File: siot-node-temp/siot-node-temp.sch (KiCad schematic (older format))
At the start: 9 parts, among them J1 Conn_01x03, J2 Conn_01x03, J3 Conn_01x03, J4 Conn_01x03, U1 L78L05_SO8

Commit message: fix hole sizes
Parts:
- J1, J4: footprint Connector_PinHeader_1.27mm:PinHeader_1x03_P1.27mm_Vertical -> bec:xConnect; symbol Connector_Generic:Conn_01x03 -> Connector:Conn_01x03_Female
- J2, J3: footprint Connector_PinHeader_1.27mm:PinHeader_1x03_P1.27mm_Vertical -> Connector_PinHeader_2.54mm:PinHeader_1x03_P2.54mm_Vertical; symbol Connector_Generic:Conn_01x03 -> Connector:Conn_01x03_Female
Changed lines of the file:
@@
 EESchema Schematic File Version 4
+LIBS:siot-node-temp-cache
 EELAYER 29 0
 EELAYER END
@@
 $EndComp
 $Comp
-L Connector_Generic:Conn_01x03 J1
+L Connector:Conn_01x03_Female J1
 U 1 1 5D321886
 P 4050 3500
 F 0 "J1" H 4200 3600 50  0000 C CNN
 F 1 "Conn_01x03" H 4050 3300 50  0000 C CNN
-F 2 "Connector_PinHeader_1.27mm:PinHeader_1x03_P1.27mm_Vertical" H 4050 3500 50  0001 C CNN
+F 2 "bec:xConnect" H 4050 3500 50  0001 C CNN
 F 3 "~" H 4050 3500 50  0001 C CNN
 	1    4050 3500
@@
 $EndComp
 $Comp
-L Connector_Generic:Conn_01x03 J4
+L Connector:Conn_01x03_Female J4
 U 1 1 5D323EF2
 P 6750 3500
 F 0 "J4" H 6830 3542 50  0000 L CNN
 F 1 "Conn_01x03" H 6550 3300 50  0000 L CNN
-F 2 "Connector_PinHeader_1.27mm:PinHeader_1x03_P1.27mm_Vertical" H 6750 3500 50  0001 C CNN
+F 2 "bec:xConnect" H 6750 3500 50  0001 C CNN
 F 3 "~" H 6750 3500 50  0001 C CNN
 	1    6750 3500
@@
 $EndComp
 $Comp
-L Connector_Generic:Conn_01x03 J2
+L Connector:Conn_01x03_Female J2
 U 1 1 5D32548C
 P 4800 2500
 F 0 "J2" V 4764 2312 50  0000 R CNN
 F 1 "Conn_01x03" V 4673 2312 50  0000 R CNN
-F 2 "Connector_PinHeader_1.27mm:PinHeader_1x03_P1.27mm_Vertical" H 4800 2500 50  0001 C CNN
+F 2 "Connector_PinHeader_2.54mm:PinHeader_1x03_P2.54mm_Vertical" H 4800 2500 50  0001 C CNN
 F 3 "~" H 4800 2500 50  0001 C CNN
 	1    4800 2500
@@
 $EndComp
 $Comp
-L Connector_Generic:Conn_01x03 J3
+L Connector:Conn_01x03_Female J3
 U 1 1 5D327365
 P 5800 2500
 F 0 "J3" V 5764 2312 50  0000 R CNN
 F 1 "Conn_01x03" V 5673 2312 50  0000 R CNN
-F 2 "Connector_PinHeader_1.27mm:PinHeader_1x03_P1.27mm_Vertical" H 5800 2500 50  0001 C CNN
+F 2 "Connector_PinHeader_2.54mm:PinHeader_1x03_P2.54mm_Vertical" H 5800 2500 50  0001 C CNN
 F 3 "~" H 5800 2500 50  0001 C CNN
 	1    5800 2500

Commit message: design updates
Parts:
- removed J1, J4: Conn_01x03, bec:xConnect, symbol Connector:Conn_01x03_Female
- removed U1: L78L05_SO8, Package_SO:SOIC-8_3.9x4.9mm_P1.27mm, symbol Regulator_Linear:L78L05_SO8
- added J1, J4: xConnect_smd, BEC:xConnect_smd, symbol bec-connector:xConnect_smd
- added U1: ADP7142AUJZ-3.3, Package_TO_SOT_SMD:TSOT-23-5, symbol Regulator_Linear:ADP7142AUJZ-3.3
- C1, C2: value 0.1uF -> 2.2uF
- J2, J3: footprint Connector_PinHeader_2.54mm:PinHeader_1x03_P2.54mm_Vertical -> BEC:1x03_solder-pads
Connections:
- net labels added: +3.3V
- net labels removed: +5V
- wire segments 31 -> 34
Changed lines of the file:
@@
 EESchema Schematic File Version 4
 LIBS:siot-node-temp-cache
-EELAYER 29 0
+EELAYER 30 0
 EELAYER END
 $Descr A 11000 8500
@@
 $EndDescr
 $Comp
-L Regulator_Linear:L78L05_SO8 U1
-U 1 1 5D31E739
-P 5450 4000
-F 0 "U1" H 5450 4242 50  0000 C CNN
-F 1 "L78L05_SO8" H 5450 4151 50  0000 C CNN
-F 2 "Package_SO:SOIC-8_3.9x4.9mm_P1.27mm" H 5550 4200 50  0001 C CIN
-F 3 "http://www.st.com/content/ccc/resource/technical/document/datasheet/15/55/e5/aa/23/5b/43/fd/CD00000446.pdf/files/CD00000446.pdf/jcr:content/translations/en.CD00000446.pdf" H 5650 4000 50  0001 C CNN
-	1    5450 4000
-	1    0    0    -1
-$EndComp
-$Comp
-L Connector:Conn_01x03_Female J1
-U 1 1 5D321886
-P 4050 3500
-F 0 "J1" H 4200 3600 50  0000 C CNN
-F 1 "Conn_01x03" H 4050 3300 50  0000 C CNN
-F 2 "bec:xConnect" H 4050 3500 50  0001 C CNN
-F 3 "~" H 4050 3500 50  0001 C CNN
-	1    4050 3500
-	-1   0    0    -1
-$EndComp
-$Comp
-L Connector:Conn_01x03_Female J4
-U 1 1 5D323EF2
-P 6750 3500
-F 0 "J4" H 6830 3542 50  0000 L CNN
-F 1 "Conn_01x03" H 6550 3300 50  0000 L CNN
-F 2 "bec:xConnect" H 6750 3500 50  0001 C CNN
-F 3 "~" H 6750 3500 50  0001 C CNN
-	1    6750 3500
-	1    0    0    -1
-$EndComp
-$Comp
 L Connector:Conn_01x03_Female J2
 U 1 1 5D32548C
@@
 F 0 "J2" V 4764 2312 50  0000 R CNN
 F 1 "Conn_01x03" V 4673 2312 50  0000 R CNN
-F 2 "Connector_PinHeader_2.54mm:PinHeader_1x03_P2.54mm_Vertical" H 4800 2500 50  0001 C CNN
+F 2 "BEC:1x03_solder-pads" H 4800 2500 50  0001 C CNN
 F 3 "~" H 4800 2500 50  0001 C CNN
 	1    4800 2500
@@
 F 0 "J3" V 5764 2312 50  0000 R CNN
 F 1 "Conn_01x03" V 5673 2312 50  0000 R CNN
-F 2 "Connector_PinHeader_2.54mm:PinHeader_1x03_P2.54mm_Vertical" H 5800 2500 50  0001 C CNN
+F 2 "BEC:1x03_solder-pads" H 5800 2500 50  0001 C CNN
 F 3 "~" H 5800 2500 50  0001 C CNN
 	1    5800 2500
@@
 Text Label 4300 3500 0    50   ~ 0
 data
-$Comp
-L power:+5V #PWR08
-U 1 1 5D32ADE6
-P 5900 3950
-F 0 "#PWR08" H 5900 3800 50  0001 C CNN
-F 1 "+5V" H 5915 4123 50  0000 C CNN
-F 2 "" H 5900 3950 50  0001 C CNN
-F 3 "" H 5900 3950 50  0001 C CNN
-	1    5900 3950
-	1    0    0    -1
-$EndComp
-Wire Wire Line
-	5750 4000 5900 4000
-Wire Wire Line
-	5900 4000 5900 3950
+Wire Wire Line
+	6350 4000 6350 3950
 $Comp
 L power:GND #PWR06
 U 1 1 5D32B611
-P 5450 4350
-F 0 "#PWR06" H 5450 4100 50  0001 C CNN
-F 1 "GND" H 5455 4177 50  0000 C CNN
-F 2 "" H 5450 4350 50  0001 C CNN
-F 3 "" H 5450 4350 50  0001 C CNN
-	1    5450 4350
-	1    0    0    -1
-$EndComp
-Wire Wire Line
-	5450 4300 5450 4350
+P 5650 4450
+F 0 "#PWR06" H 5650 4200 50  0001 C CNN
+F 1 "GND" H 5655 4277 50  0000 C CNN
+F 2 "" H 5650 4450 50  0001 C CNN
+F 3 "" H 5650 4450 50  0001 C CNN
+	1    5650 4450
+	1    0    0    -1
+$EndComp
+Wire Wire Line
+	5650 4400 5650 4450
 Wire Wire Line
 	4400 3400 6550 3400
@@
 	4950 3950 4950 4000
 Wire Wire Line
-	4950 4000 5150 4000
-$Comp
-L power:+5V #PWR03
-U 1 1 5D32C4FA
-P 4450 2700
-F 0 "#PWR03" H 4450 2550 50  0001 C CNN
-F 1 "+5V" H 4465 2873 50  0000 C CNN
-F 2 "" H 4450 2700 50  0001 C CNN
-F 3 "" H 4450 2700 50  0001 C CNN
-	1    4450 2700
-	1    0    0    -1
-$EndComp
+	4950 4000 5250 4000
 Wire Wire Line
 	4450 2700 4450 2750
@@
 P 4950 4300
 F 0 "C1" H 5065 4346 50  0000 L CNN
-F 1 "0.1uF" H 5065 4255 50  0000 L CNN
+F 1 "2.2uF" H 5065 4255 50  0000 L CNN
 F 2 "Capacitor_SMD:C_0603_1608Metric" H 4988 4150 50  0001 C CNN
 F 3 "~" H 4950 4300 50  0001 C CNN
@@
 L Device:C C2
 U 1 1 5D330CD0
-P 5900 4300
-F 0 "C2" H 6015 4346 50  0000 L CNN
-F 1 "0.1uF" H 6015 4255 50  0000 L CNN
-F 2 "Capacitor_SMD:C_0603_1608Metric" H 5938 4150 50  0001 C CNN
-F 3 "~" H 5900 4300 50  0001 C CNN
-	1    5900 4300
+P 6350 4300
+F 0 "C2" H 6465 4346 50  0000 L CNN
+F 1 "2.2uF" H 6465 4255 50  0000 L CNN
+F 2 "Capacitor_SMD:C_0603_1608Metric" H 6388 4150 50  0001 C CNN
+F 3 "~" H 6350 4300 50  0001 C CNN
+	1    6350 4300
 	1    0    0    -1
 $EndComp
@@
 Connection ~ 4950 4000
 Wire Wire Line
-	5900 4000 5900 4150
-Connection ~ 5900 4000
+	6350 4000 6350 4150
+Connection ~ 6350 4000
 $Comp
 L power:GND #PWR05
@@
 L power:GND #PWR09
 U 1 1 5D3334E3
-P 5900 4500
-F 0 "#PWR09" H 5900 4250 50  0001 C CNN
-F 1 "GND" H 5905 4327 50  0000 C CNN
-F 2 "" H 5900 4500 50  0001 C CNN
-F 3 "" H 5900 4500 50  0001 C CNN
-	1    5900 4500
+P 6350 4500
+F 0 "#PWR09" H 6350 4250 50  0001 C CNN
+F 1 "GND" H 6355 4327 50  0000 C CNN
+F 2 "" H 6350 4500 50  0001 C CNN
+F 3 "" H 6350 4500 50  0001 C CNN
+	1    6350 4500
 	1    0    0    -1
 $EndComp
@@
 	4950 4450 4950 4500
 Wire Wire Line
-	5900 4450 5900 4500
+	6350 4450 6350 4500
+$Comp
+L bec-connector:xConnect_smd J1
+U 1 1 5D689C19
+P 4050 3500
+F 0 "J1" H 4050 3850 50  0000 C CNN
+F 1 "xConnect_smd" H 4050 3750 50  0000 C CNN
+F 2 "BEC:xConnect_smd" H 4000 3250 50  0001 C CNN
+F 3 "~" H 4050 3500 50  0001 C CNN
+	1    4050 3500
+	-1   0    0    -1
+$EndComp
+$Comp
+L bec-connector:xConnect_smd J4
+U 1 1 5D68A579
+P 6750 3500
+F 0 "J4" H 6750 3850 50  0000 C CNN
+F 1 "xConnect_smd" H 6750 3750 50  0000 C CNN
+F 2 "BEC:xConnect_smd" H 6700 3250 50  0001 C CNN
+F 3 "~" H 6750 3500 50  0001 C CNN
+	1    6750 3500
+	1    0    0    -1
+$EndComp
+$Comp
+L Regulator_Linear:ADP7142AUJZ-3.3 U1
+U 1 1 5D68AE2A
+P 5650 4100
+F 0 "U1" H 5650 4467 50  0000 C CNN
+F 1 "ADP7142AUJZ-3.3" H 5650 4376 50  0000 C CNN
+F 2 "Package_TO_SOT_SMD:TSOT-23-5" H 5650 3700 50  0001 C CIN
+F 3 "https://www.analog.com/media/en/technical-documentation/data-sheets/ADP7142.pdf" H 5650 3600 50  0001 C CNN
+	1    5650 4100
+	1    0    0    -1
+$EndComp
+Wire Wire Line
+	6050 4000 6200 4000
+Wire Wire Line
+	6200 4100 6200 4000
+Wire Wire Line
+	6050 4100 6200 4100
+Connection ~ 6200 4000
+Wire Wire Line
+	6200 4000 6350 4000
+$Comp
+L power:+3.3V #PWR0101
+U 1 1 5D693774
+P 6350 3950
+F 0 "#PWR0101" H 6350 3800 50  0001 C CNN
+F 1 "+3.3V" H 6365 4123 50  0000 C CNN
+F 2 "" H 6350 3950 50  0001 C CNN
+F 3 "" H 6350 3950 50  0001 C CNN
+	1    6350 3950
+	1    0    0    -1
+$EndComp
+$Comp
+L power:+3.3V #PWR0102
+U 1 1 5D693C5B
+P 4450 2700
+F 0 "#PWR0102" H 4450 2550 50  0001 C CNN
+F 1 "+3.3V" H 4465 2873 50  0000 C CNN
+F 2 "" H 4450 2700 50  0001 C CNN
+F 3 "" H 4450 2700 50  0001 C CNN
+	1    4450 2700
+	1    0    0    -1
+$EndComp
 $EndSCHEMATC

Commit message: update PNs on symbols
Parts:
- C1, C2: value 2.2uF -> 2.2uF_50V; footprint Capacitor_SMD:C_0603_1608Metric -> Capacitor_SMD:C_2220_5650Metric; symbol Device:C -> bec-passive:2.2uF_50V; MPN (none) -> GRM188R61H225ME11J; Manufacturer (none) -> Murata
- U1: symbol Regulator_Linear:ADP7142AUJZ-3.3 -> bec-power:ADP7142AUJZ-3.3; MPN (none) -> ADP7142AUJZ-3.3; Manufacturer (none) -> Analog Devices
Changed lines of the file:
@@
 	5800 3500 6550 3500
 $Comp
-L Device:C C1
+L bec-passive:2.2uF_50V C1
 U 1 1 5D330621
 P 4950 4300
 F 0 "C1" H 5065 4346 50  0000 L CNN
-F 1 "2.2uF" H 5065 4255 50  0000 L CNN
-F 2 "Capacitor_SMD:C_0603_1608Metric" H 4988 4150 50  0001 C CNN
-F 3 "~" H 4950 4300 50  0001 C CNN
+F 1 "2.2uF_50V" H 5065 4255 50  0000 L CNN
+F 2 "Capacitor_SMD:C_2220_5650Metric" H 4988 4150 50  0001 C CNN
+F 3 "https://product.tdk.com/info/en/catalog/datasheets/mlcc_commercial_midvoltage_en.pdf" H 4950 4300 50  0001 C CNN
+F 4 "GRM188R61H225ME11J" H 4950 4300 50  0001 C CNN "MPN"
+F 5 "Murata" H 4950 4300 50  0001 C CNN "Manufacturer"
 	1    4950 4300
 	1    0    0    -1
 $EndComp
 $Comp
-L Device:C C2
+L bec-passive:2.2uF_50V C2
 U 1 1 5D330CD0
 P 6350 4300
 F 0 "C2" H 6465 4346 50  0000 L CNN
-F 1 "2.2uF" H 6465 4255 50  0000 L CNN
-F 2 "Capacitor_SMD:C_0603_1608Metric" H 6388 4150 50  0001 C CNN
-F 3 "~" H 6350 4300 50  0001 C CNN
+F 1 "2.2uF_50V" H 6465 4255 50  0000 L CNN
+F 2 "Capacitor_SMD:C_2220_5650Metric" H 6388 4150 50  0001 C CNN
+F 3 "https://product.tdk.com/info/en/catalog/datasheets/mlcc_commercial_midvoltage_en.pdf" H 6350 4300 50  0001 C CNN
+F 4 "GRM188R61H225ME11J" H 6350 4300 50  0001 C CNN "MPN"
+F 5 "Murata" H 6350 4300 50  0001 C CNN "Manufacturer"
 	1    6350 4300
 	1    0    0    -1
@@
 $EndComp
 $Comp
-L Regulator_Linear:ADP7142AUJZ-3.3 U1
+L bec-power:ADP7142AUJZ-3.3 U1
 U 1 1 5D68AE2A
 P 5650 4100
@@
 F 2 "Package_TO_SOT_SMD:TSOT-23-5" H 5650 3700 50  0001 C CIN
 F 3 "https://www.analog.com/media/en/technical-documentation/data-sheets/ADP7142.pdf" H 5650 3600 50  0001 C CNN
+F 4 "ADP7142AUJZ-3.3" H 5650 4100 50  0001 C CNN "MPN"
+F 5 "Analog Devices" H 5650 4100 50  0001 C CNN "Manufacturer"
 	1    5650 4100
 	1    0    0    -1

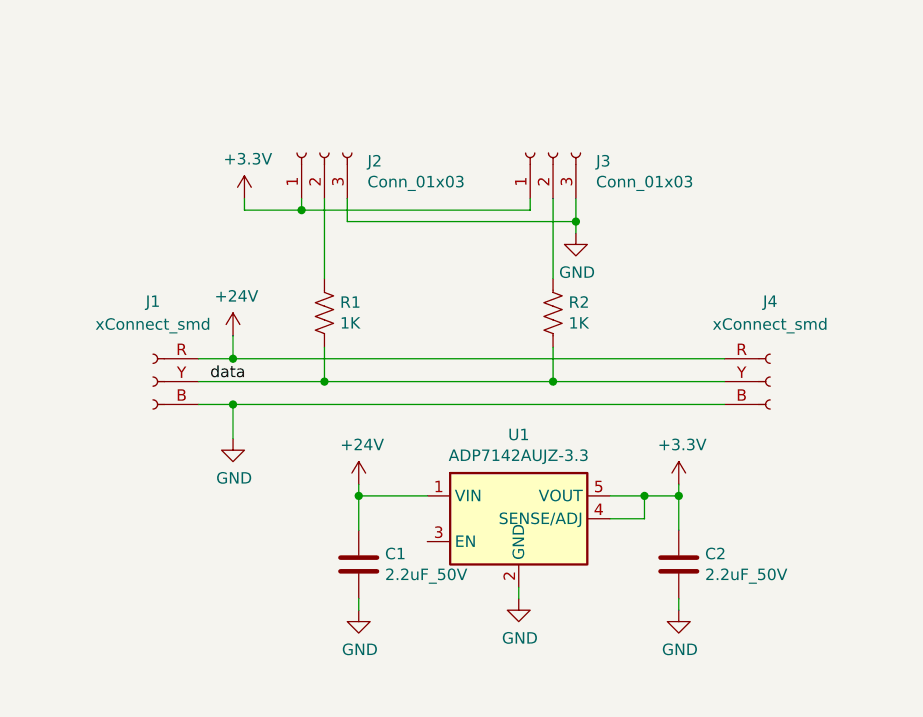
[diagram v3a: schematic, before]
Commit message: fix missing en on temp board
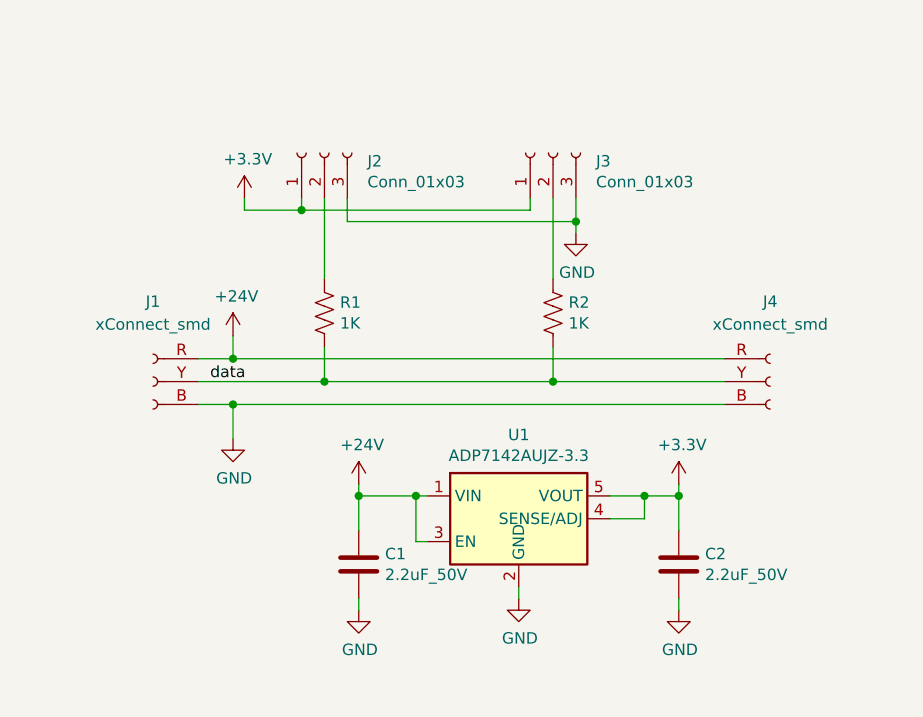
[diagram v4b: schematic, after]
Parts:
- C1, C2: footprint Capacitor_SMD:C_2220_5650Metric -> Capacitor_SMD:C_0603_1608Metric
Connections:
- net +24V: now also U1.3 (EN)
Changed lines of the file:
@@
 	4950 3950 4950 4000
 Wire Wire Line
-	4950 4000 5250 4000
+	4950 4000 5200 4000
 Wire Wire Line
 	4450 2700 4450 2750
@@
 F 0 "C1" H 5065 4346 50  0000 L CNN
 F 1 "2.2uF_50V" H 5065 4255 50  0000 L CNN
-F 2 "Capacitor_SMD:C_2220_5650Metric" H 4988 4150 50  0001 C CNN
+F 2 "Capacitor_SMD:C_0603_1608Metric" H 4988 4150 50  0001 C CNN
 F 3 "https://product.tdk.com/info/en/catalog/datasheets/mlcc_commercial_midvoltage_en.pdf" H 4950 4300 50  0001 C CNN
 F 4 "GRM188R61H225ME11J" H 4950 4300 50  0001 C CNN "MPN"
@@
 F 0 "C2" H 6465 4346 50  0000 L CNN
 F 1 "2.2uF_50V" H 6465 4255 50  0000 L CNN
-F 2 "Capacitor_SMD:C_2220_5650Metric" H 6388 4150 50  0001 C CNN
+F 2 "Capacitor_SMD:C_0603_1608Metric" H 6388 4150 50  0001 C CNN
 F 3 "https://product.tdk.com/info/en/catalog/datasheets/mlcc_commercial_midvoltage_en.pdf" H 6350 4300 50  0001 C CNN
 F 4 "GRM188R61H225ME11J" H 6350 4300 50  0001 C CNN "MPN"
@@
 	1    0    0    -1
 $EndComp
+Wire Wire Line
+	5200 4000 5200 4200
+Wire Wire Line
+	5200 4200 5250 4200
+Connection ~ 5200 4000
+Wire Wire Line
+	5200 4000 5250 4000
 $EndSCHEMATC

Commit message: updates
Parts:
- R1, R2: value 1K -> 100
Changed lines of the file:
@@
 P 4800 3200
 F 0 "R1" H 4868 3246 50  0000 L CNN
-F 1 "1K" H 4868 3155 50  0000 L CNN
+F 1 "100" H 4868 3155 50  0000 L CNN
 F 2 "Resistor_SMD:R_0603_1608Metric" V 4840 3190 50  0001 C CNN
 F 3 "~" H 4800 3200 50  0001 C CNN
@@
 P 5800 3200
 F 0 "R2" H 5868 3246 50  0000 L CNN
-F 1 "1K" H 5868 3155 50  0000 L CNN
+F 1 "100" H 5868 3155 50  0000 L CNN
 F 2 "Resistor_SMD:R_0603_1608Metric" V 5840 3190 50  0001 C CNN
 F 3 "~" H 5800 3200 50  0001 C CNN

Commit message: temp node tweaks
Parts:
- U1: value ADP7142AUJZ-3.3 -> ADP7142AUJZ-5.0; symbol bec-power:ADP7142AUJZ-3.3 -> bec-power:ADP7142AUJZ-5.0; MPN ADP7142AUJZ-3.3 -> ADP7142AUJZ-5.0
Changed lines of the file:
@@
 $EndComp
 $Comp
-L bec-power:ADP7142AUJZ-3.3 U1
+L bec-power:ADP7142AUJZ-5.0 U1
 U 1 1 5D68AE2A
 P 5650 4100
 F 0 "U1" H 5650 4467 50  0000 C CNN
-F 1 "ADP7142AUJZ-3.3" H 5650 4376 50  0000 C CNN
+F 1 "ADP7142AUJZ-5.0" H 5650 4376 50  0000 C CNN
 F 2 "Package_TO_SOT_SMD:TSOT-23-5" H 5650 3700 50  0001 C CIN
 F 3 "https://www.analog.com/media/en/technical-documentation/data-sheets/ADP7142.pdf" H 5650 3600 50  0001 C CNN
-F 4 "ADP7142AUJZ-3.3" H 5650 4100 50  0001 C CNN "MPN"
+F 4 "ADP7142AUJZ-5.0" H 5650 4100 50  0001 C CNN "MPN"
 F 5 "Analog Devices" H 5650 4100 50  0001 C CNN "Manufacturer"
 	1    5650 4100

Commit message: updates
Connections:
- net +3V3 renamed +5V
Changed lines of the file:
@@
 Wire Wire Line
 	6200 4000 6350 4000
-$Comp
-L power:+3.3V #PWR0101
-U 1 1 5D693774
-P 6350 3950
-F 0 "#PWR0101" H 6350 3800 50  0001 C CNN
-F 1 "+3.3V" H 6365 4123 50  0000 C CNN
-F 2 "" H 6350 3950 50  0001 C CNN
-F 3 "" H 6350 3950 50  0001 C CNN
-	1    6350 3950
-	1    0    0    -1
-$EndComp
-$Comp
-L power:+3.3V #PWR0102
-U 1 1 5D693C5B
-P 4450 2700
-F 0 "#PWR0102" H 4450 2550 50  0001 C CNN
-F 1 "+3.3V" H 4465 2873 50  0000 C CNN
-F 2 "" H 4450 2700 50  0001 C CNN
-F 3 "" H 4450 2700 50  0001 C CNN
-	1    4450 2700
-	1    0    0    -1
-$EndComp
 Wire Wire Line
 	5200 4000 5200 4200
@@
 Wire Wire Line
 	5200 4000 5250 4000
+$Comp
+L power:+5V #PWR?
+U 1 1 5DCE3829
+P 4450 2700
+F 0 "#PWR?" H 4450 2550 50  0001 C CNN
+F 1 "+5V" H 4465 2873 50  0000 C CNN
+F 2 "" H 4450 2700 50  0001 C CNN
+F 3 "" H 4450 2700 50  0001 C CNN
+	1    4450 2700
+	1    0    0    -1
+$EndComp
+$Comp
+L power:+5V #PWR?
+U 1 1 5DCE3E5A
+P 6350 3950
+F 0 "#PWR?" H 6350 3800 50  0001 C CNN
+F 1 "+5V" H 6365 4123 50  0000 C CNN
+F 2 "" H 6350 3950 50  0001 C CNN
+F 3 "" H 6350 3950 50  0001 C CNN
+	1    6350 3950
+	1    0    0    -1
+$EndComp
 $EndSCHEMATC
